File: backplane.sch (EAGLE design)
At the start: 45 parts, among them J1 L717HDE15PD4CH4R, J10 5013310807, J11 5013310807, J12 5013310807, J13 5013310807, J14 5013311007, J15 5013311007, J16 5013311007, J17 5013311007, J18 5013311007, J19 5013311007, J2 1054301102, J20 5013311007, J21 5013311007, J22 5013311007, J23 5013311007, J24 SEAM-40-03.0-S-06-2-A-K-TR, J25 5055670271, J3 5011902017, J4 5013310807, J5 5013310807, J6 5013310807, J7 5013310807, J8 5013310807, J9 5013310807, U1 AM26LV32EIPWR, U10 AM26LV32EIPWR, U2 AM26LV32EIPWR, U3 AM26LV32EIPWR, U4 AM26LV32EIPWR, U5 AM26LV32EIPWR, U6 AM26LV32EIPWR, U7 AM26LV32EIPWR, U8 AM26LV32EIPWR, U9 AM26LV32EIPWR

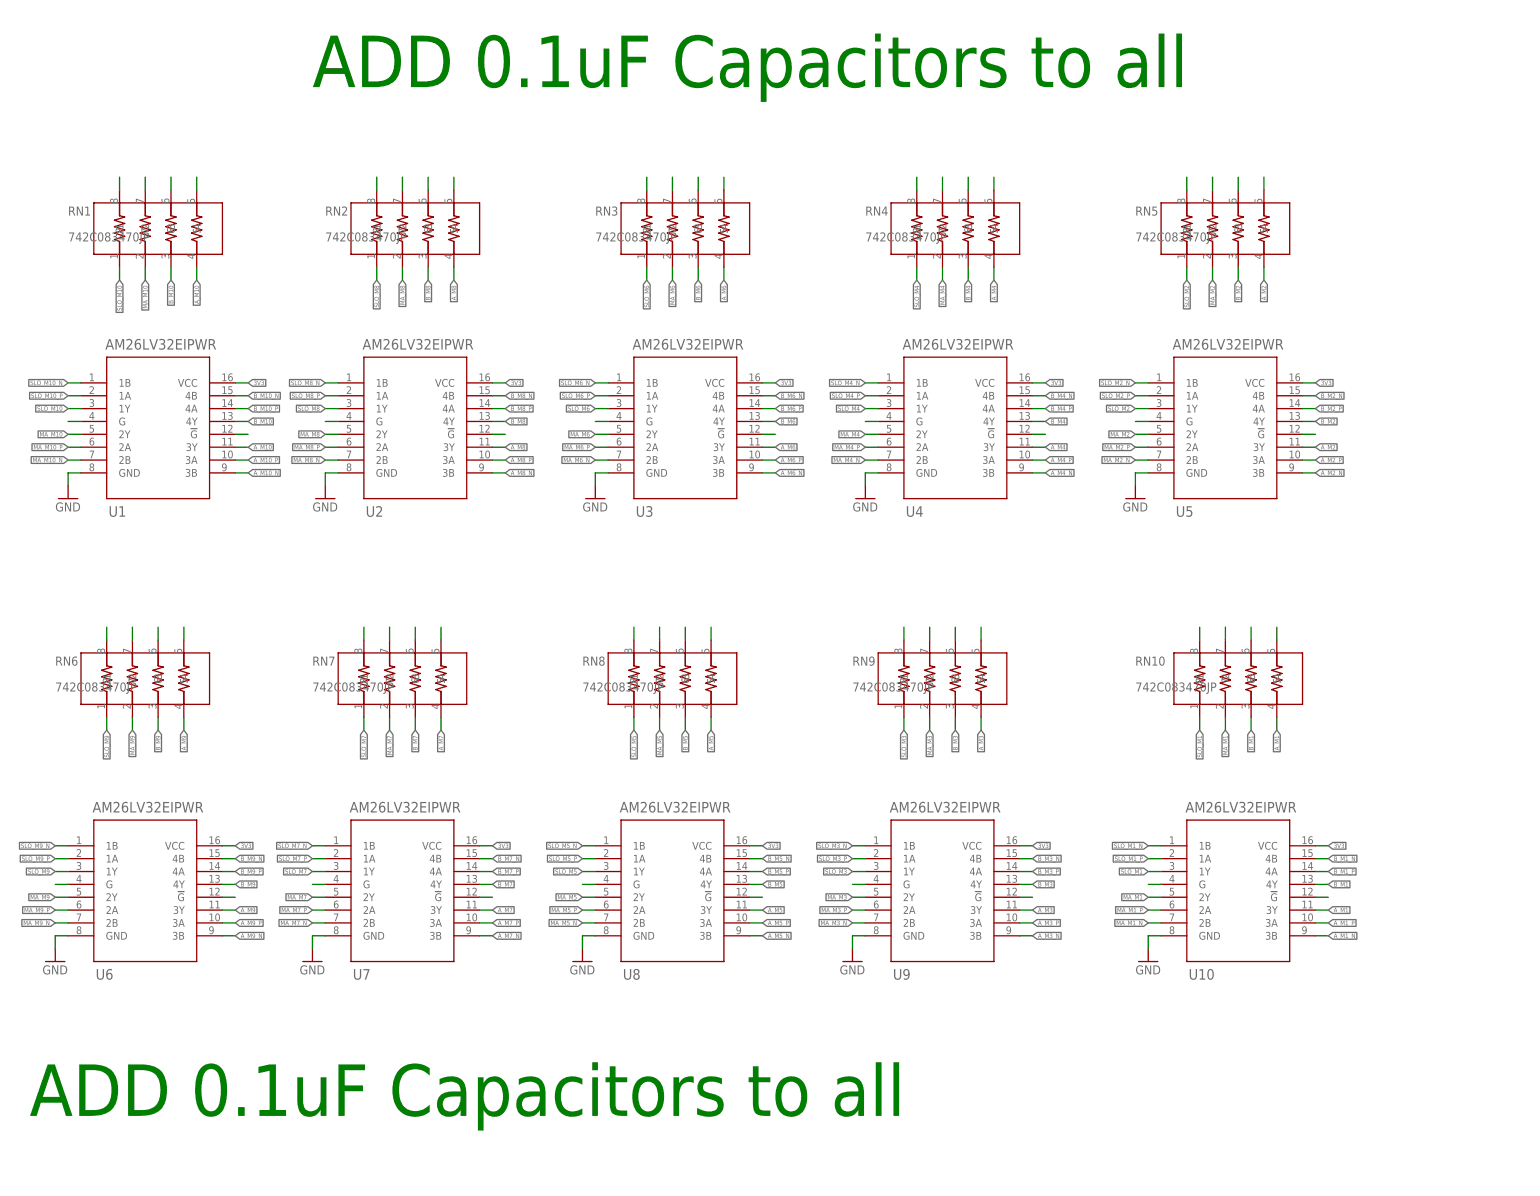
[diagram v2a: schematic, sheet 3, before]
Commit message: adjusted silkscreen
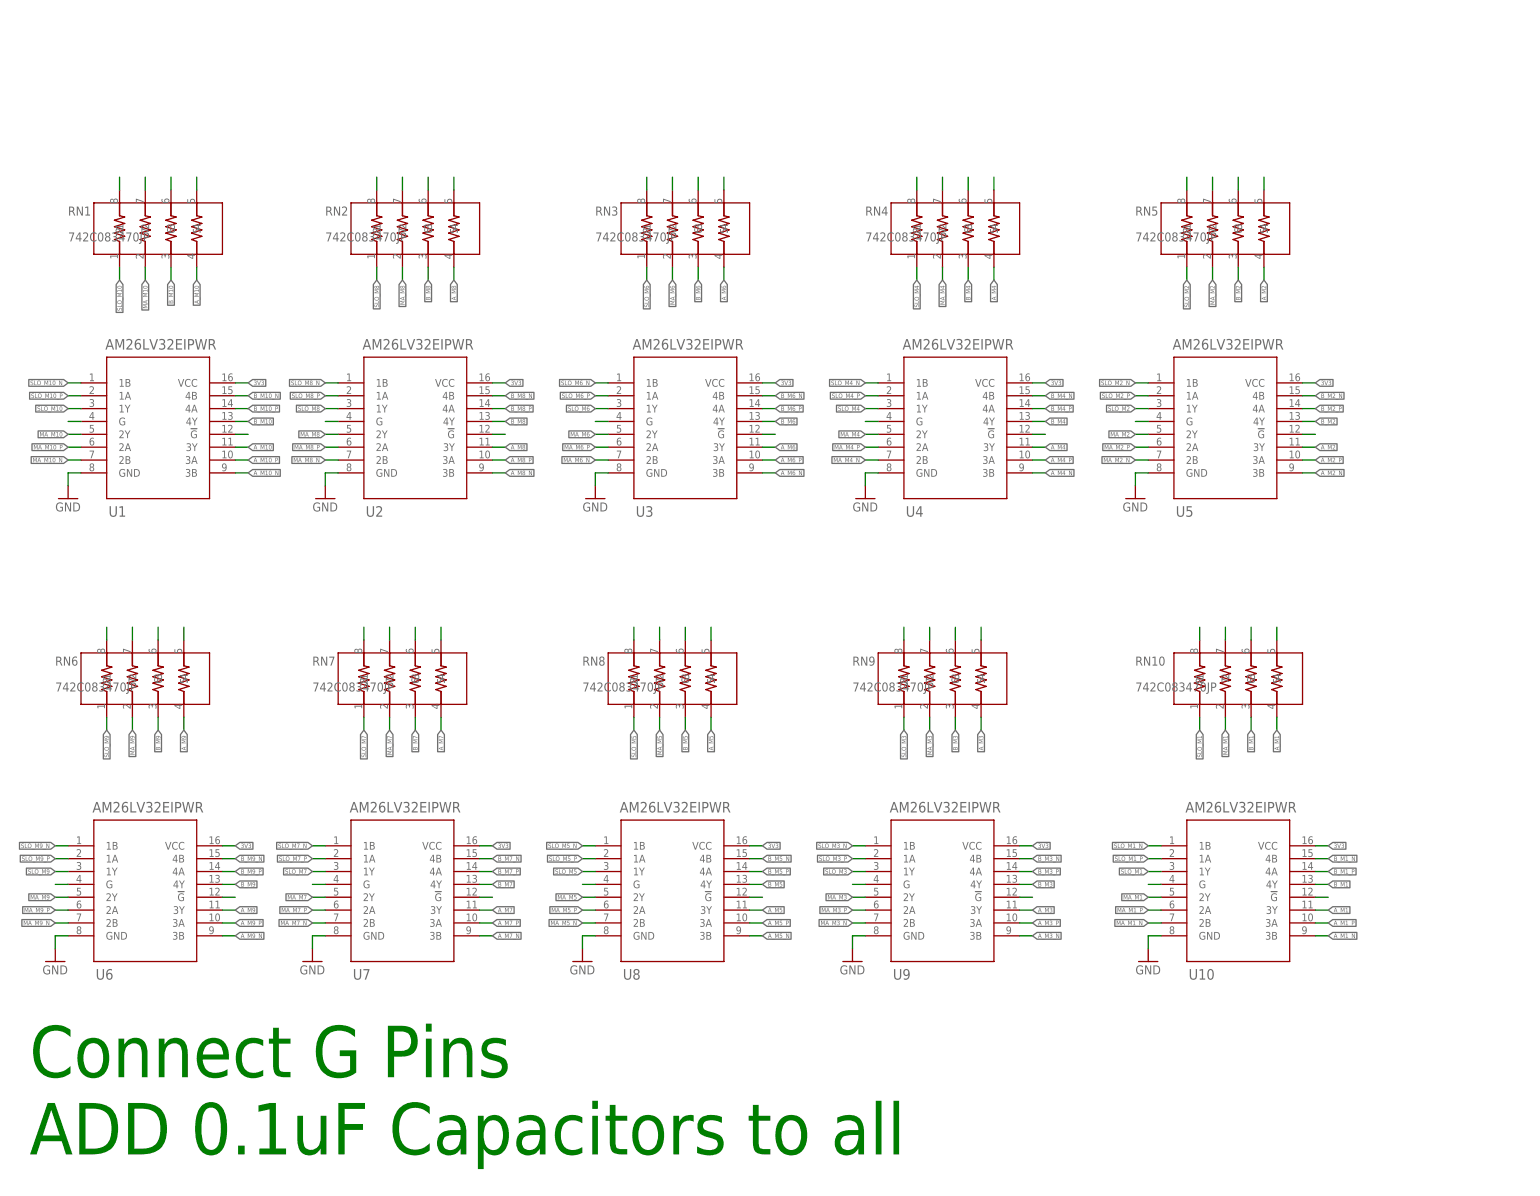
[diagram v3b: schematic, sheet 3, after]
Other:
- note added: "Connect G Pins"
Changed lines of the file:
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@@
 <sheet>
 <plain>
-<text x="66.04" y="215.9" size="10.16" layer="91">ADD 0.1uF Capacitors to all</text>
-<text x="10.16" y="12.7" size="10.16" layer="91">ADD 0.1uF Capacitors to all</text>
+<text x="10.16" y="20.32" size="10.16" layer="91">Connect G Pins</text>
+<text x="10.16" y="5.08" size="10.16" layer="91">ADD 0.1uF Capacitors to all</text>
 </plain>
 <instances>

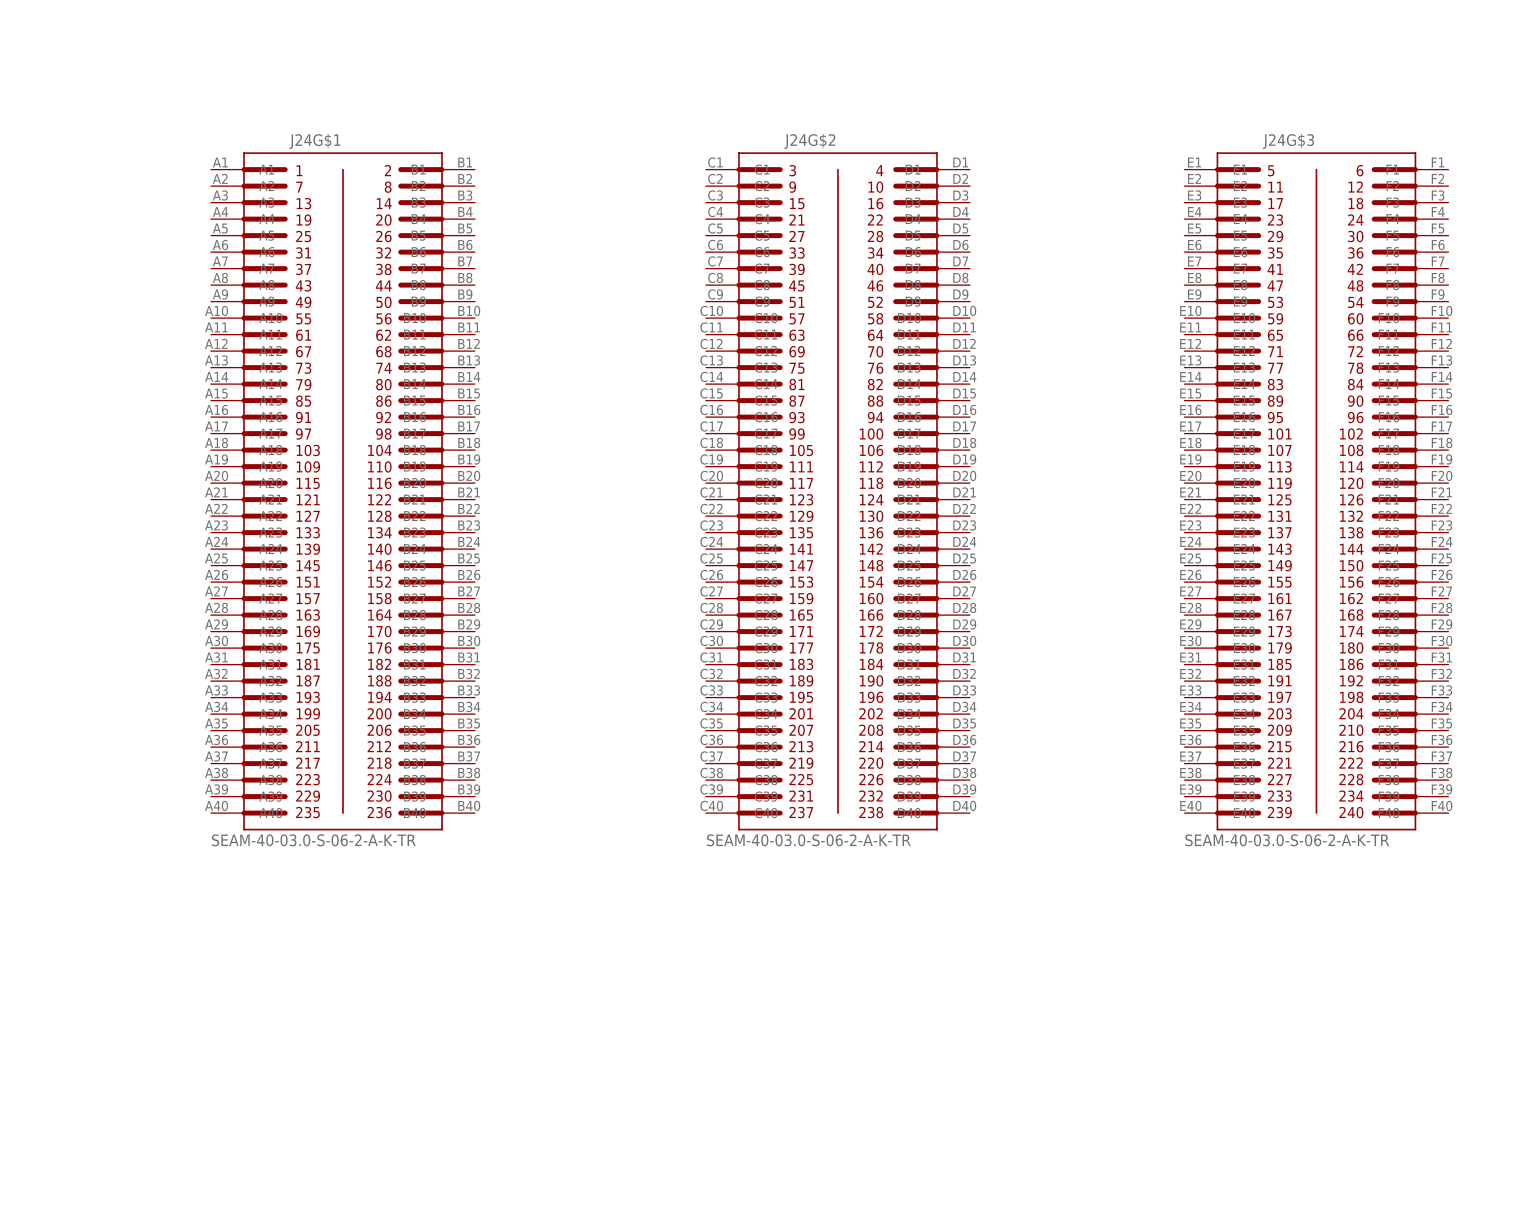
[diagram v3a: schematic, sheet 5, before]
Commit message: many RMC connections routed
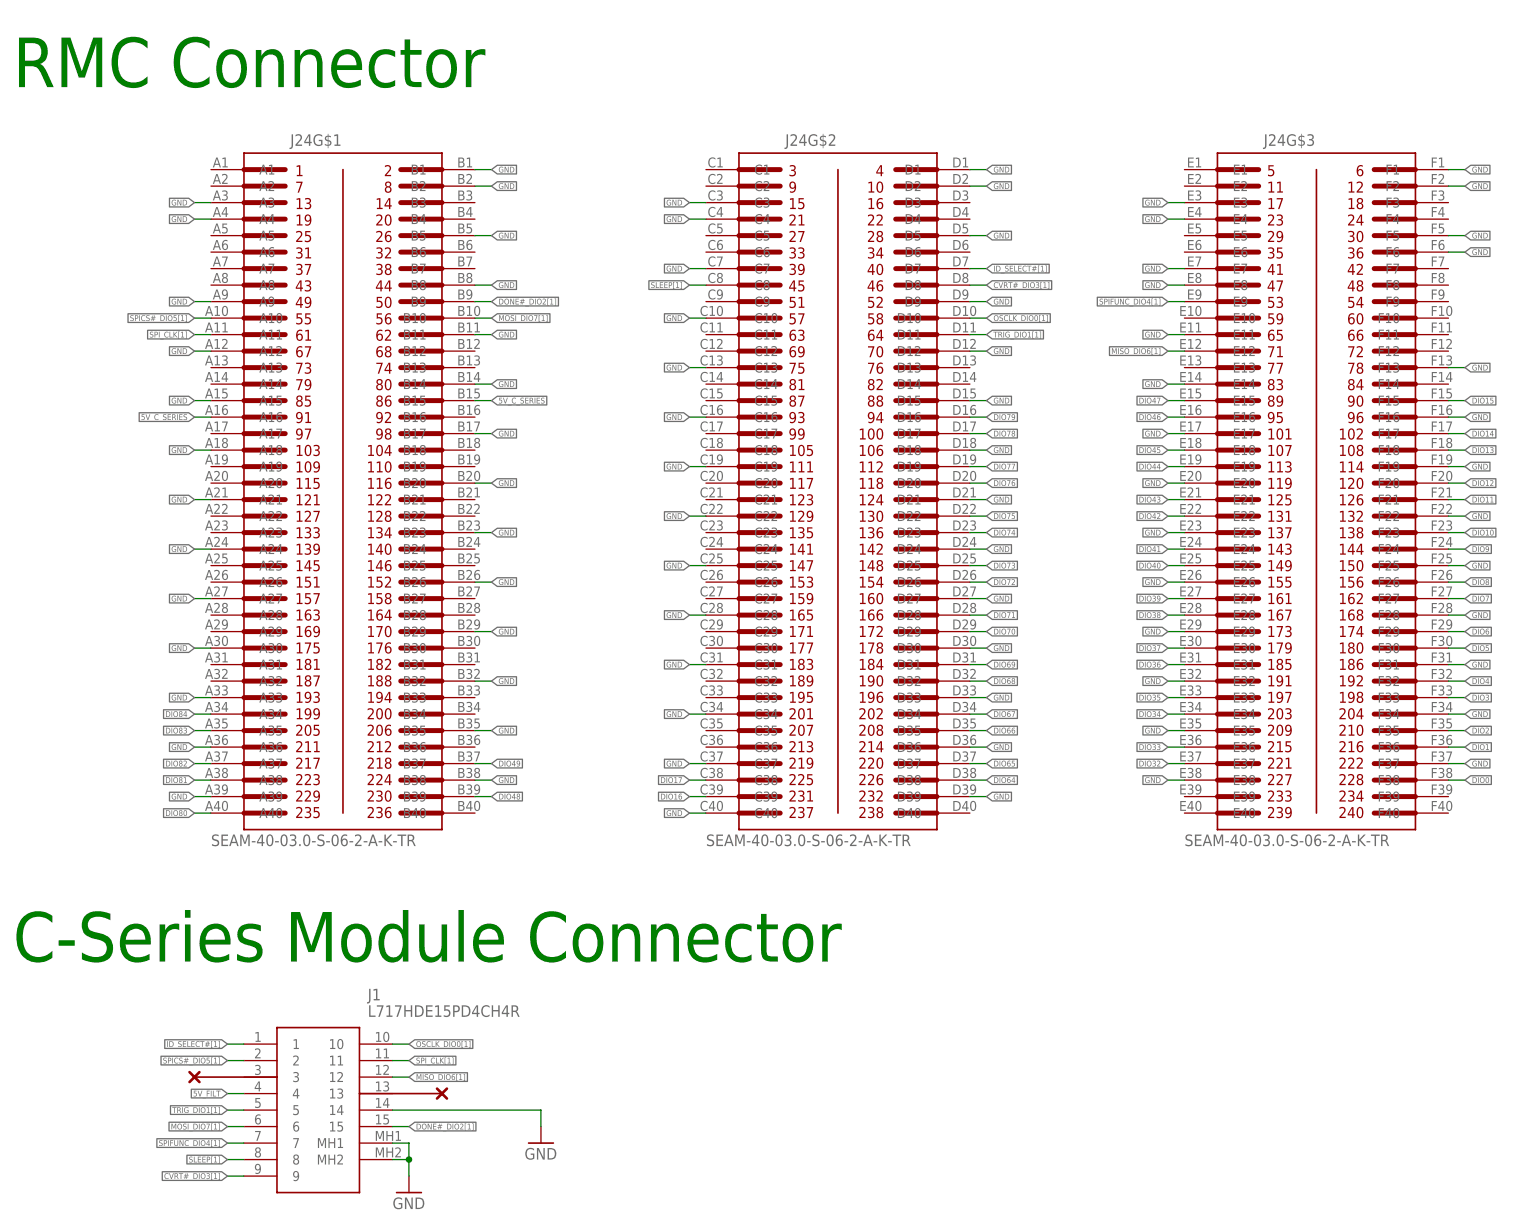
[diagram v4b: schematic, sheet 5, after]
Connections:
- new net 5V_C_SERIES: J24G$1.A16, J24G$1.B15
- new net 5V_FILT: J1.4
- new net CVRT#_DIO3[1]: J1.9, J24G$2.D8
- new net DIO0: J24G$3.F38
- new net DIO1: J24G$3.F36
- new net DIO10: J24G$3.F23
- new net DIO11: J24G$3.F21
- new net DIO12: J24G$3.F20
- new net DIO13: J24G$3.F18
- new net DIO14: J24G$3.F17
- new net DIO15: J24G$3.F15
- new net DIO16: J24G$2.C39
- new net DIO17: J24G$2.C38
- new net DIO2: J24G$3.F35
- new net DIO3: J24G$3.F33
- new net DIO32: J24G$3.E37
- new net DIO33: J24G$3.E36
- new net DIO34: J24G$3.E34
- new net DIO35: J24G$3.E33
- new net DIO36: J24G$3.E31
- new net DIO37: J24G$3.E30
- new net DIO38: J24G$3.E28
- new net DIO39: J24G$3.E27
- new net DIO4: J24G$3.F32
- new net DIO40: J24G$3.E25
- new net DIO41: J24G$3.E24
- new net DIO42: J24G$3.E22
- new net DIO43: J24G$3.E21
- new net DIO44: J24G$3.E19
- new net DIO45: J24G$3.E18
- new net DIO46: J24G$3.E16
- new net DIO47: J24G$3.E15
- new net DIO48: J24G$1.B39
- new net DIO49: J24G$1.B37
- new net DIO5: J24G$3.F30
- new net DIO6: J24G$3.F29
- new net DIO64: J24G$2.D38
- new net DIO65: J24G$2.D37
- new net DIO66: J24G$2.D35
- new net DIO67: J24G$2.D34
- new net DIO68: J24G$2.D32
- new net DIO69: J24G$2.D31
- new net DIO7: J24G$3.F27
- new net DIO70: J24G$2.D29
- new net DIO71: J24G$2.D28
- new net DIO72: J24G$2.D26
- new net DIO73: J24G$2.D25
- new net DIO74: J24G$2.D23
- new net DIO75: J24G$2.D22
- new net DIO76: J24G$2.D20
- new net DIO77: J24G$2.D19
- new net DIO78: J24G$2.D17
- new net DIO79: J24G$2.D16
- new net DIO8: J24G$3.F26
- new net DIO80: J24G$1.A40
- new net DIO81: J24G$1.A38
- new net DIO82: J24G$1.A37
- new net DIO83: J24G$1.A35
- new net DIO84: J24G$1.A34
- new net DIO9: J24G$3.F24
- new net DONE#_DIO2[1]: J1.15, J24G$1.B9
- new net ID_SELECT#[1]: J1.1, J24G$2.D7
- new net MISO_DIO6[1]: J1.12, J24G$3.E12
- new net MOSI_DIO7[1]: J1.6, J24G$1.B10
- new net OSCLK_DIO0[1]: J1.10, J24G$2.D10
- new net SLEEP[1]: J1.8, J24G$2.C8
- new net SPICS#_DIO5[1]: J1.2, J24G$1.A10
- new net SPIFUNC_DIO4[1]: J1.7, J24G$3.E9
- new net SPI_CLK[1]: J1.11, J24G$1.A11
- new net TRIG_DIO1[1]: J1.5, J24G$2.D11
- net GND: now also J1.14, J1.MH1, J1.MH2, J24G$1.A12, J24G$1.A15, J24G$1.A18, J24G$1.A21, J24G$1.A24, J24G$1.A27, J24G$1.A3, J24G$1.A30, J24G$1.A33, J24G$1.A36, J24G$1.A39, J24G$1.A4, J24G$1.A9, J24G$1.B1, J24G$1.B11, J24G$1.B14, J24G$1.B17, J24G$1.B2, J24G$1.B20, J24G$1.B23, J24G$1.B26, J24G$1.B29, J24G$1.B32, J24G$1.B35, J24G$1.B38, J24G$1.B5, J24G$1.B8, J24G$2.C10, J24G$2.C13, J24G$2.C16, J24G$2.C19, J24G$2.C22, J24G$2.C25, J24G$2.C28, J24G$2.C3, J24G$2.C31, J24G$2.C34, J24G$2.C37, J24G$2.C4, J24G$2.C40, J24G$2.C7, J24G$2.D1, J24G$2.D12, J24G$2.D15, J24G$2.D18, J24G$2.D2, J24G$2.D21, J24G$2.D24, J24G$2.D27, J24G$2.D30, J24G$2.D33, J24G$2.D36, J24G$2.D39, J24G$2.D5, J24G$2.D9, J24G$3.E11, J24G$3.E14, J24G$3.E17, J24G$3.E20, J24G$3.E23, J24G$3.E26, J24G$3.E29, J24G$3.E3, J24G$3.E32, J24G$3.E35, J24G$3.E38, J24G$3.E4, J24G$3.E7, J24G$3.E8, J24G$3.F1, J24G$3.F13, J24G$3.F16, J24G$3.F19, J24G$3.F2, J24G$3.F22, J24G$3.F25, J24G$3.F28, J24G$3.F31, J24G$3.F34, J24G$3.F37, J24G$3.F5, J24G$3.F6
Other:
- note added: "AMC Driver and Encoder Connectors"
- note added: "Analog In"
- note added: "C-Series Module Connector"
- note added: "RMC Connector"
